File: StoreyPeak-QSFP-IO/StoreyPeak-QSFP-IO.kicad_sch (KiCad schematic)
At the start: 35 parts, among them U1 QSFP_PCB-QSFP, U2 XC6206P62xMR, U3 CH340G, X1 X322512MSB4SI

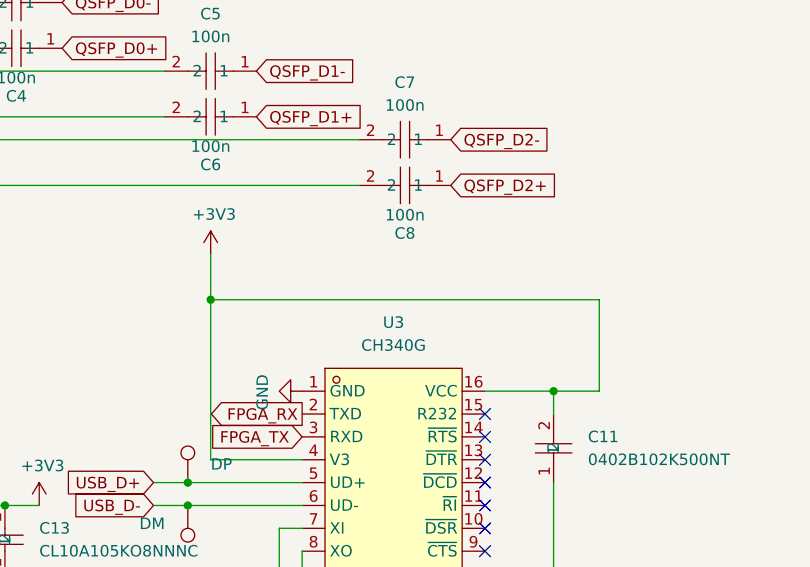
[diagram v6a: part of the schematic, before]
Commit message: Readd 3V3 test point
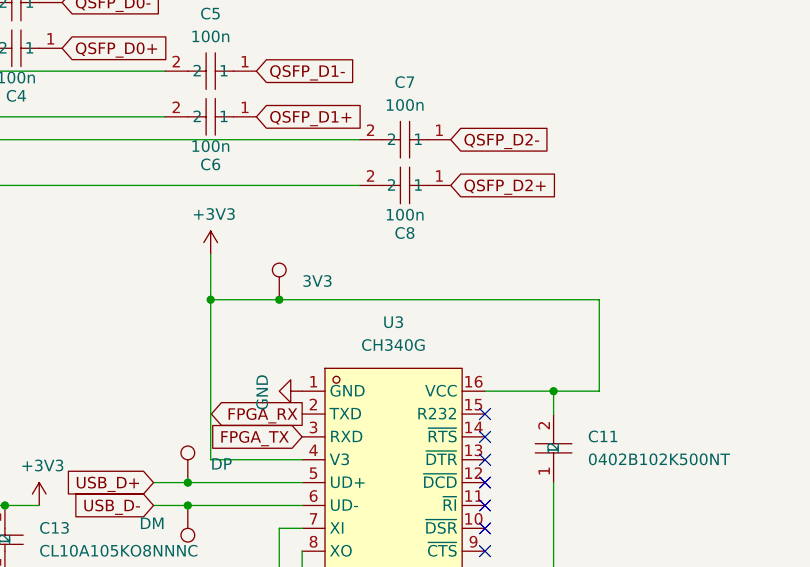
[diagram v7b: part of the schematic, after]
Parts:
- added TP8: 3V3, TestPoint:TestPoint_Pad_1.5x1.5mm, symbol Connector:TestPoint
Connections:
- net +3V3: now also TP8.1
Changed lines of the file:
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@@
 	)
 	(junction
+		(at 146.05 93.98)
+		(diameter 0)
+		(color 0 0 0 0)
+	)
+	(junction
 		(at 255.27 133.35)
 		(diameter 0)
@@
 	(wire
 		(pts
+			(xy 146.05 93.98) (xy 181.61 93.98)
+		)
+		(stroke
+			(width 0)
+			(type default)
+		)
+	)
+	(wire
+		(pts
 			(xy 69.85 17.78) (xy 16.51 17.78)
 		)
@@
 	(wire
 		(pts
-			(xy 138.43 93.98) (xy 181.61 93.98)
+			(xy 138.43 93.98) (xy 146.05 93.98)
 		)
 		(stroke
@@
 					(unit 1)
 				)
+			)
+		)
+	)
+	(symbol
+		(lib_id "Connector:TestPoint")
+		(at 146.05 93.98 0)
+		(unit 1)
+		(exclude_from_sim no)
+		(in_bom yes)
+		(on_board yes)
+		(dnp no)
+		(property "Reference" "TP8"
+			(at 148.59 89.4079 0)
+			(effects
+				(font
+					(size 1.27 1.27)
+				)
+				(justify left)
+				(hide yes)
+			)
+		)
+		(property "Value" "3V3"
+			(at 148.59 91.9479 0)
+			(effects
+				(font
+					(size 1.27 1.27)
+				)
+				(justify left)
+			)
+		)
+		(property "Footprint" "TestPoint:TestPoint_Pad_1.5x1.5mm"
+			(at 151.13 93.98 0)
+			(effects
+				(font
+					(size 1.27 1.27)
+				)
+				(hide yes)
+			)
+		)
+		(property "Datasheet" "~"
+			(at 151.13 93.98 0)
+			(effects
+				(font
+					(size 1.27 1.27)
+				)
+				(hide yes)
+			)
+		)
+		(property "Description" "test point"
+			(at 146.05 93.98 0)
+			(effects
+				(font
+					(size 1.27 1.27)
+				)
+				(hide yes)
+			)
+		)
+		(pin "1"
+		)
+		(instances
+			(project "StoreyPeak-QSFP-IO"
+				(path "/09a4c8ee-e8d7-4980-8dc1-43a8ae75179d"
+					(reference "TP8")
+					(unit 1)
+				)
